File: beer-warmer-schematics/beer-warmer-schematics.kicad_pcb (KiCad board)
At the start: 4 copper layers, 60 x 42.8 mm, 45 parts, among them J1 USB_C_Receptacle_6P, J2 Screw_Terminal_01x02, J3 Conn_01x07_Socket, J4 Conn_01x07_Socket, J5 Conn_01x04_Pin, J6 Screw_Terminal_01x03, J7 Conn_01x07_Socket, J8 Conn_01x07_Socket, Q1 AOD4184A, U2 TPS5430DDA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

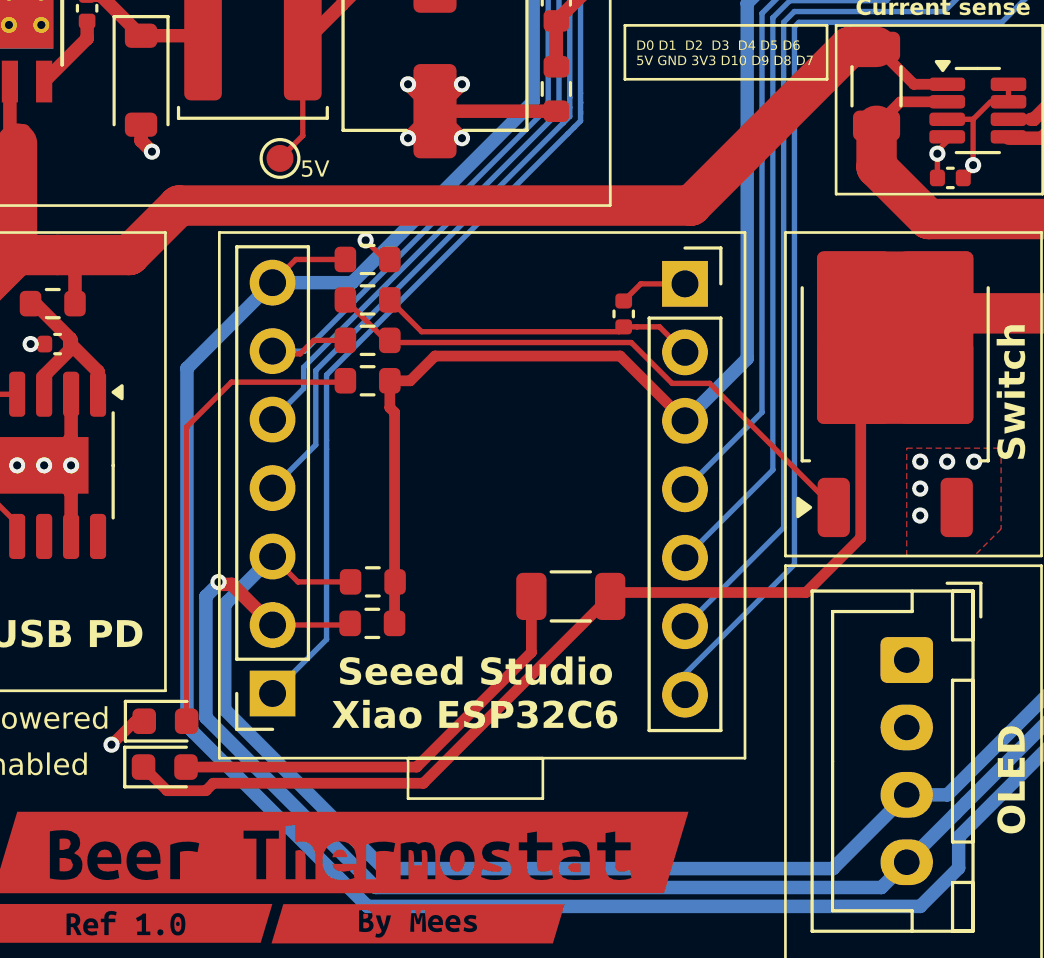
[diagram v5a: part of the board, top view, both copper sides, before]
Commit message: active led in parallel with load
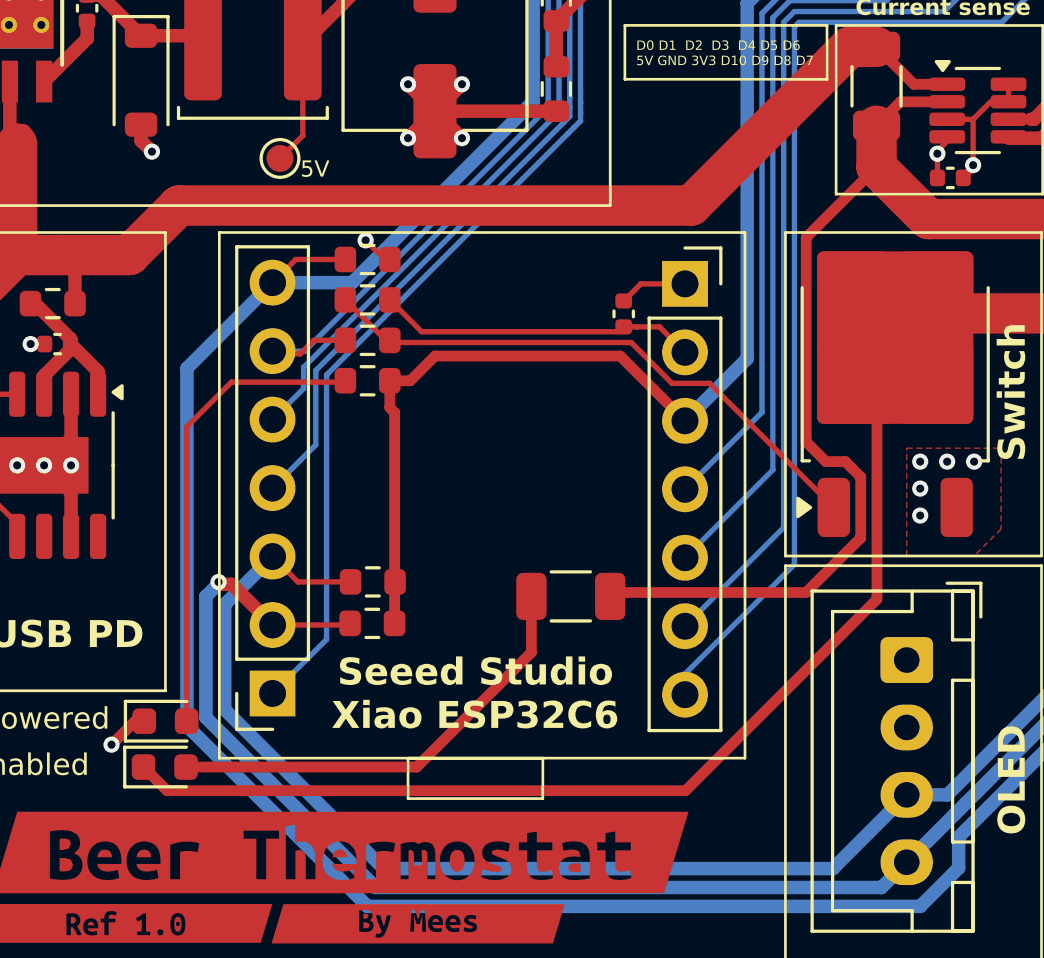
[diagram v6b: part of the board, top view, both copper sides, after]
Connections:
- R3 pad 1: HEAT- -> HEAT+
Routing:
- net HEAT+: track 17.7 -> 44.0 mm
- net HEAT-: track 59.7 -> 61.9 mm
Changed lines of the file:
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@@
 		(tags "Through hole pin header THT 1x07 2.54mm single row")
 		(property "Reference" "J8"
-			(at 0 -2.33 90)
+			(at 0 -2.33 270)
 			(layer "F.SilkS")
 			(hide yes)
@@
 		)
 		(property "Value" "Conn_01x07_Socket"
-			(at 0 17.57 90)
+			(at 0 17.57 270)
 			(layer "F.Fab")
 			(effects
@@
 		(sheetname "/")
 		(sheetfile "beer-warmer-schematics.kicad_sch")
-		(attr through_hole)
+		(attr through_hole exclude_from_bom)
 		(fp_line
 			(start -1.8 17.05)
@@
 		)
 		(embedded_fonts no)
+		(model "${KICAD9_3DMODEL_DIR}/Connector_PinHeader_2.54mm.3dshapes/PinHeader_1x07_P2.54mm_Vertical.wrl"
+			(offset
+				(xyz 0 0 0)
+			)
+			(scale
+				(xyz 1 1 1)
+			)
+			(rotate
+				(xyz 0 0 0)
+			)
+		)
 	)
 	(footprint "MountingHole:MountingHole_3.2mm_M3_DIN965_Pad"
@@
 		(sheetname "/")
 		(sheetfile "beer-warmer-schematics.kicad_sch")
-		(attr through_hole)
+		(attr through_hole exclude_from_bom)
 		(fp_line
 			(start 1.8 -1.8)
@@
 		)
 		(fp_text user "${REFERENCE}"
-			(at 0 7.62 0)
+			(at 0 7.62 180)
 			(layer "F.Fab")
 			(effects
@@
 		)
 		(embedded_fonts no)
+		(model "${KICAD9_3DMODEL_DIR}/Connector_PinHeader_2.54mm.3dshapes/PinHeader_1x07_P2.54mm_Vertical.wrl"
+			(offset
+				(xyz 0 0 0)
+			)
+			(scale
+				(xyz 1 1 1)
+			)
+			(rotate
+				(xyz 0 0 0)
+			)
+		)
 	)
 	(footprint "Package_SO:TI_SO-PowerPAD-8_ThermalVias"
@@
 			(layers "F.Cu" "F.Mask" "F.Paste")
 			(roundrect_rratio 0.222222)
-			(net 22 "HEAT-")
+			(net 21 "HEAT+")
 			(pintype "passive")
 		)
@@
 	)
 	(segment
+		(start 152.645662 100.354338)
+		(end 159.765742 100.354338)
+		(width 0.4)
+		(layer "F.Cu")
+		(net 21)
+	)
+	(segment
+		(start 159.7715 94.7715)
+		(end 159.7715 87.182848)
+		(width 0.4)
+		(layer "F.Cu")
+		(net 21)
+	)
+	(segment
+		(start 161.7935 96.07342)
+		(end 161.22008 95.5)
+		(width 0.4)
+		(layer "F.Cu")
+		(net 21)
+	)
+	(segment
 		(start 163.268527 82.15)
 		(end 162.38003 83.038497)
@@
 	)
 	(segment
+		(start 159.7715 87.182848)
+		(end 162.38003 84.574318)
+		(width 0.4)
+		(layer "F.Cu")
+		(net 21)
+	)
+	(segment
+		(start 161.7935 98.32658)
+		(end 161.7935 96.07342)
+		(width 0.4)
+		(layer "F.Cu")
+		(net 21)
+	)
+	(segment
 		(start 164.305712 86.5)
 		(end 169 86.5)
@@
 	)
 	(segment
+		(start 160.5 95.5)
+		(end 159.7715 94.7715)
+		(width 0.4)
+		(layer "F.Cu")
+		(net 21)
+	)
+	(segment
+		(start 161.22008 95.5)
+		(end 160.5 95.5)
+		(width 0.4)
+		(layer "F.Cu")
+		(net 21)
+	)
+	(segment
 		(start 162.38003 84.574318)
 		(end 164.305712 86.5)
@@
 	)
 	(segment
-		(start 161.5475 92.575)
-		(end 161.7935 92.821)
+		(start 152.5 100.5)
+		(end 152.645662 100.354338)
 		(width 0.4)
 		(layer "F.Cu")
-		(net 22)
+		(net 21)
 	)
 	(segment
-		(start 177.5 88.5)
-		(end 177.5 84.965)
-		(width 1.5)
+		(start 159.765742 100.354338)
+		(end 161.7935 98.32658)
+		(width 0.4)
 		(layer "F.Cu")
-		(net 22)
+		(net 21)
 	)
 	(segment
-		(start 145.569306 107.430694)
-		(end 137.775 107.430694)
+		(start 155.294306 107.705694)
+		(end 136.062665 107.705694)
 		(width 0.4)
 		(layer "F.Cu")
@@
 	)
 	(segment
-		(start 137.5 107.705694)
-		(end 136.062665 107.705694)
-		(width 0.4)
+		(start 177.5 88.5)
+		(end 177.5 84.965)
+		(width 1.5)
 		(layer "F.Cu")
 		(net 22)
 	)
 	(segment
-		(start 161.5475 89.225)
-		(end 160.716162 90.056338)
-		(width 0.2)
+		(start 162.3945 93.422)
+		(end 162.3945 100.6055)
+		(width 0.4)
 		(layer "F.Cu")
 		(net 22)
 	)
 	(segment
-		(start 152.5 100.5)
-		(end 145.569306 107.430694)
-		(width 0.4)
+		(start 161.5475 89.225)
+		(end 160.716162 90.056338)
+		(width 0.2)
 		(layer "F.Cu")
 		(net 22)
@@
 	)
 	(segment
-		(start 161.7935 98.32658)
-		(end 159.765742 100.354338)
+		(start 136.062665 107.705694)
+		(end 135.186665 106.829694)
 		(width 0.4)
 		(layer "F.Cu")
@@
 	)
 	(segment
-		(start 161.7935 92.821)
-		(end 161.7935 98.32658)
-		(width 0.4)
-		(layer "F.Cu")
-		(net 22)
-	)
-	(segment
-		(start 137.775 107.430694)
-		(end 137.5 107.705694)
-		(width 0.4)
-		(layer "F.Cu")
-		(net 22)
-	)
-	(segment
-		(start 159.765742 100.354338)
-		(end 152.645662 100.354338)
-		(width 0.4)
-		(layer "F.Cu")
-		(net 22)
-	)
-	(segment
 		(start 176 90)
 		(end 177.5 88.5)
@@
 	)
 	(segment
-		(start 136.062665 107.705694)
-		(end 135.186665 106.829694)
+		(start 161.5475 92.575)
+		(end 162.3945 93.422)
 		(width 0.4)
 		(layer "F.Cu")
@@
 	)
 	(segment
-		(start 152.645662 100.354338)
-		(end 152.5 100.5)
+		(start 162.3945 100.6055)
+		(end 155.294306 107.705694)
 		(width 0.4)
 		(layer "F.Cu")

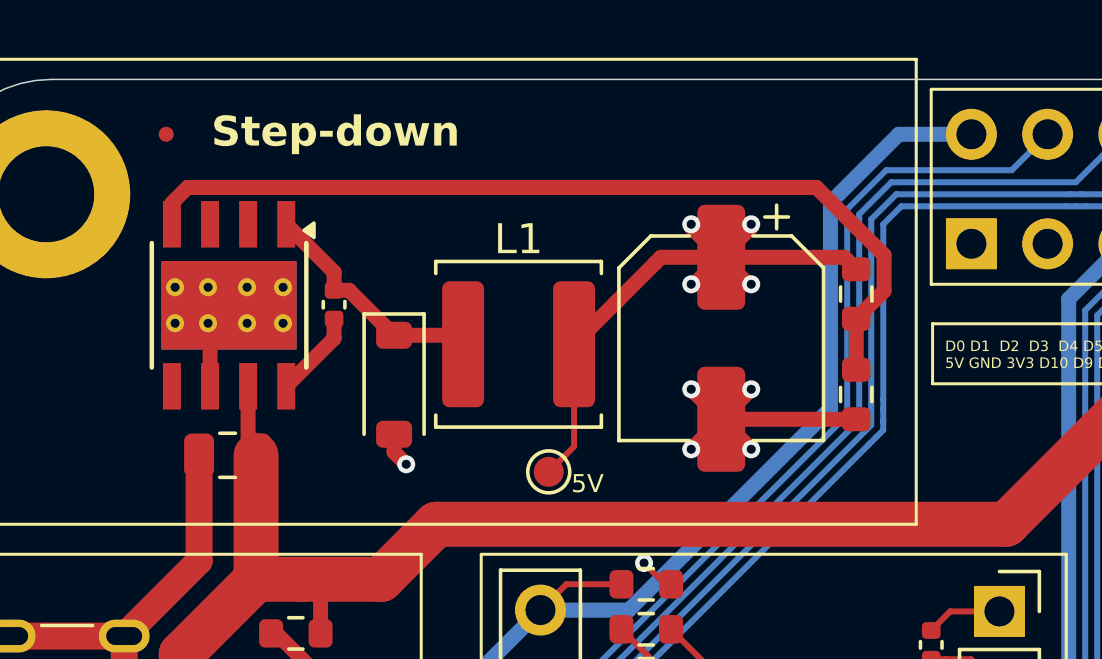
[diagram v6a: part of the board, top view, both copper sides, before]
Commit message: change diode on buck
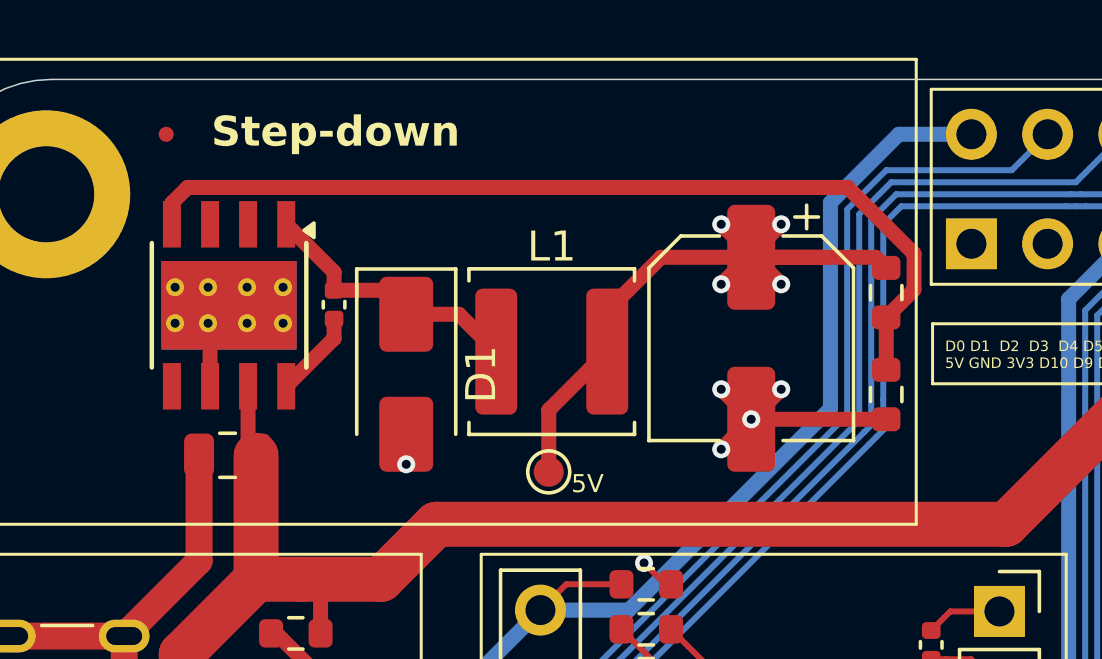
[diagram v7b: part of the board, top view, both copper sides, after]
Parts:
- D1: footprint Diode_SMD:D_SOD-123 -> Diode_SMD:D_SMA
- moved L1 1.13 mm to (140.3, 80.2)
- moved R5 1.00 mm to (151.5, 78.3)
- moved C3 1.00 mm to (147.0, 79.8)
- moved R11 1.00 mm to (151.5, 81.7)
- moved D1 0.54 mm to (135.5, 81.0)
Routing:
- net +5V: track 26.4 -> 28.2 mm
- net GND: track 65.9 -> 64.4 mm
- net Net-(D1-K): track 7.91 -> 9.11 mm
- net Net-(U2-VSENSE): track 29.8 -> 30.8 mm

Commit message: updated with new knowledge gained
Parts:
- removed TP1: TestPoint, TestPoint:TestPoint_Pad_D1.0mm
- added J9: Conn_01x02, Connector_PinHeader_2.54mm:PinHeader_1x02_P2.54mm_Vertical, F.Cu at (124.0, 81.0)
- R3: value 620R -> 200R; footprint Resistor_SMD:R_1206_3216Metric -> Resistor_SMD:R_0603_1608Metric
- moved R3 9.76 mm to (143.6, 94.2)
- moved C2 0.30 mm to (129.5, 84.0)
- moved R9 0.14 mm to (143.6, 100.0)
- moved R8 0.12 mm to (143.6, 101.5)
- moved R2 0.05 mm to (143.6, 89.5)
- moved R4 0.05 mm to (143.6, 88.0)
- moved R6 0.05 mm to (143.6, 92.5)
- moved R7 0.05 mm to (143.6, 91.0)
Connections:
- net +3V3 renamed +3.3V
- net D0 renamed /TEMP_PROBE
- net D1 renamed /HEAT_OUT
- net Net-(J4-Pin_4) renamed /<NO NET>
- net SCL renamed /SCL
- net SDA renamed /SDA
- net VDD renamed Net-(U3-CFG3)
- D2 pad 1: HEAT- -> GND
- J2 pad 1: HEAT+ -> /HEAT+
- J2 pad 2: HEAT- -> Net-(J2-Pin_2)
- J4 pad 5: Net-(J4-Pin_5) -> /LED_OUT
- J8 pad 5: Net-(J4-Pin_5) -> /LED_OUT
- Q1 pad 2: HEAT- -> Net-(J2-Pin_2)
- R10 pad 2: HEAT+ -> /HEAT+
- R3 pad 1: HEAT+ -> Net-(D2-A)
- R3 pad 2: Net-(D2-A) -> /LED_OUT
- U4 pad 2: HEAT+ -> /HEAT+
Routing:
- net HEAT-: track 61.9 -> 0.00 mm
- net HEAT+: track 44.0 -> 0.00 mm
- net /LED_OUT: track 0.00 -> 35.5 mm
- net Net-(J4-Pin_5): track 32.6 -> 0.00 mm
- net Net-(J2-Pin_2): track 0.00 -> 23.2 mm
- net /HEAT+: track 0.00 -> 17.7 mm
- net GND: track 64.4 -> 70.8 mm, vias 16 -> 19
- net +5V: track 28.2 -> 29.6 mm
- net Net-(D2-A): track 16.9 -> 17.6 mm
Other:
- board text added: "+"
- board text added: "12V out"
- board text removed: "12V"
